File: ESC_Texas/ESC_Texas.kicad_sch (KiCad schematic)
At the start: 77 parts, among them IC1 nRF52840-QFAA-F-R7, IC11 LM3480IM3-3.3_NOPB, IC12 LM3480IM3-3.3_NOPB, J1 RJ45, J11 Battery+, J12 Conn_01x02, J13 Conn_01x04_Pin, J14 Conn_01x01_Pin, J15 Conn_01x01_Pin, J16 Conn_01x01_Pin, J17 Conn_01x01_Pin, J2 BD125-10-A-0305-0580-L-B, J3 Motor, J4 Battery+, P0.10 TestPoint, P0.11 TestPoint, P0.12 TestPoint, P0.7 TestPoint, P0.9 TestPoint, P1.0 TestPoint, P1.1 TestPoint, P1.9 TestPoint, U1 MCP2515-xSO, U2 TJA1051T, X1 CM7V-T1A-32.768kHz, X2 32MHz, X3 C115962

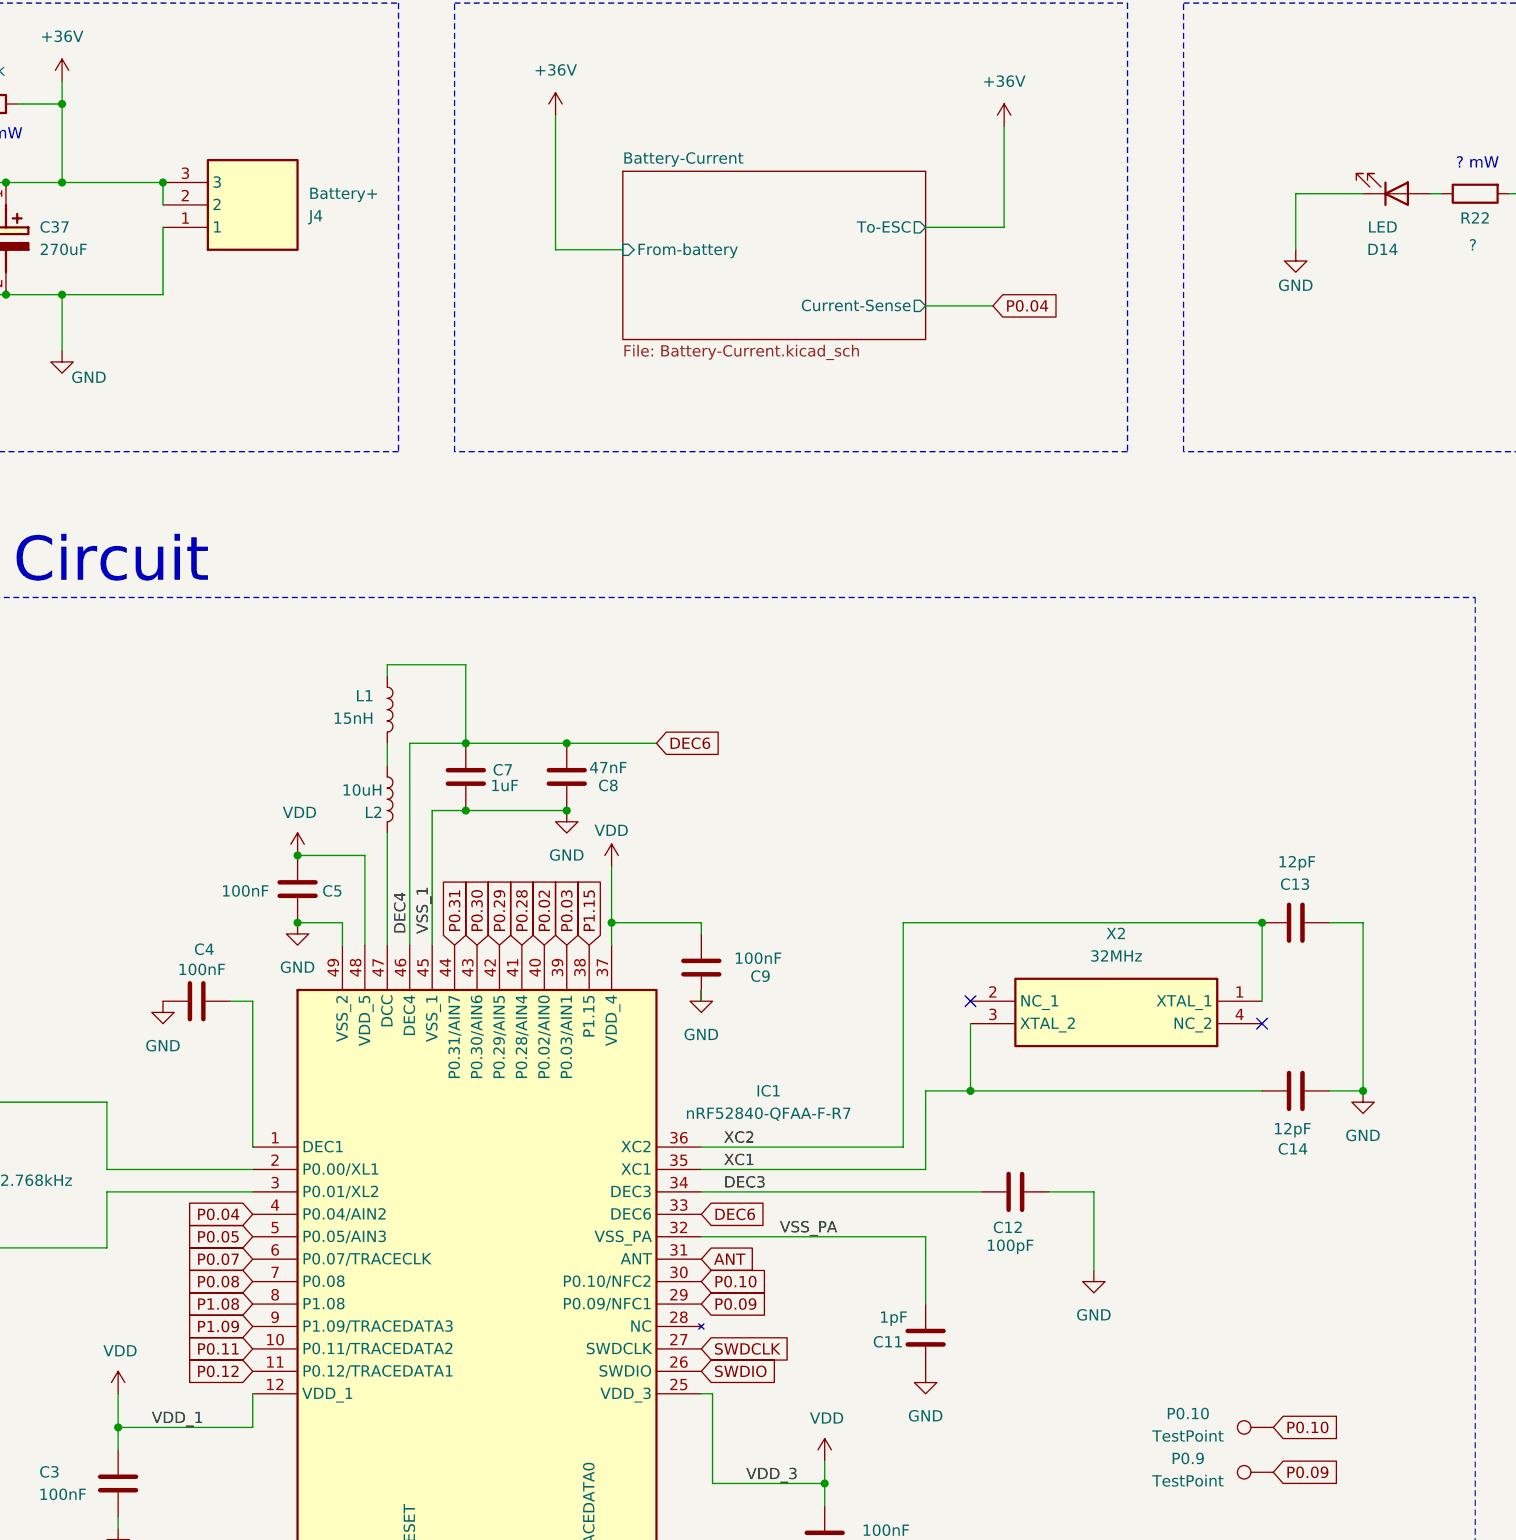
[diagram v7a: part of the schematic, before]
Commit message: Battery connector added
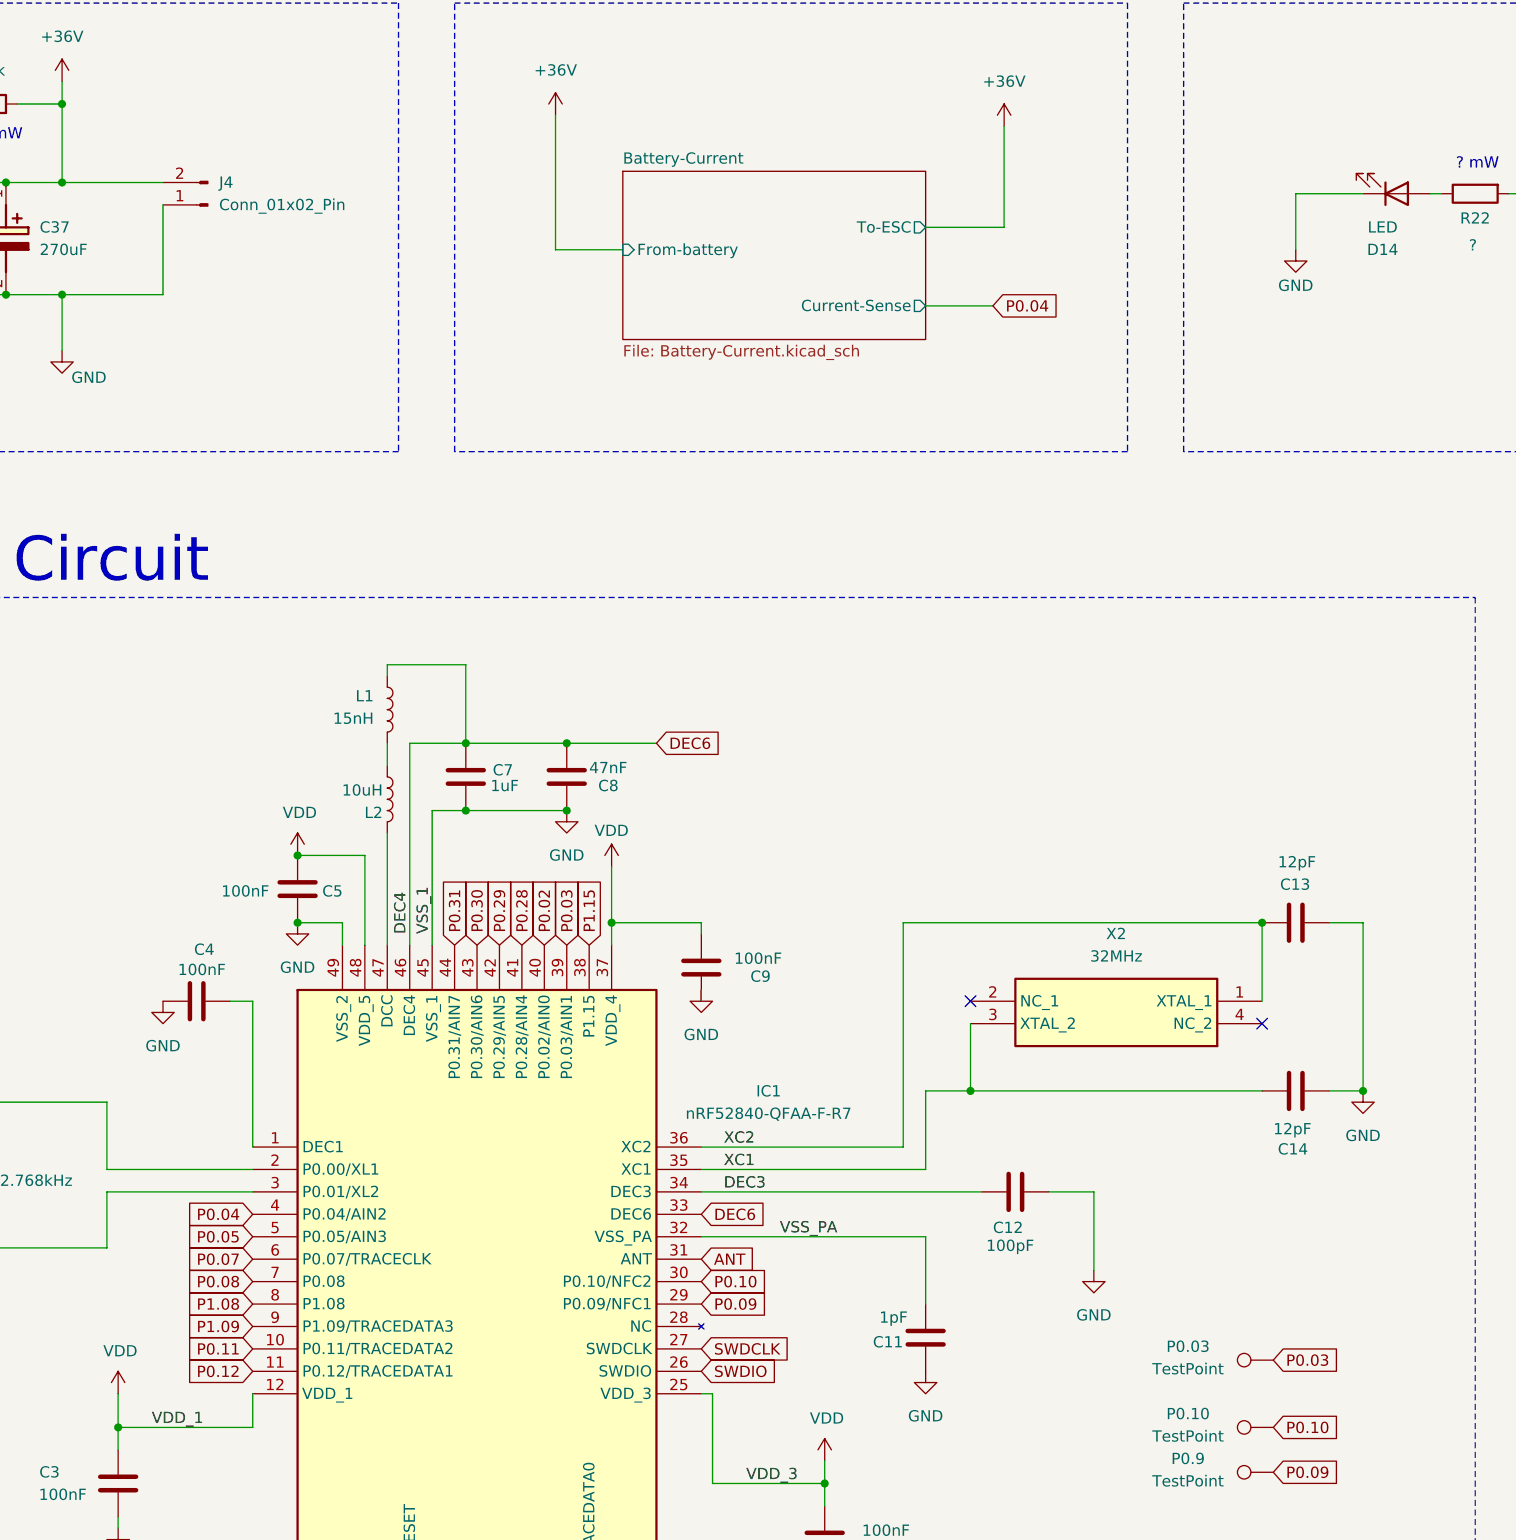
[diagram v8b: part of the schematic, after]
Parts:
- removed J4: Battery+, LIB_2350514-3:SHDRRA3W90P0X350_1X3_1110X920X691P, symbol 2350514-3:2350514-3
- added J4: Conn_01x02_Pin, MP011776:MP011776, symbol Connector:Conn_01x02_Pin
- added P0.03: TestPoint, TestPoint:TestPoint_Pad_D1.0mm, symbol Connector:TestPoint
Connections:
- net +36V: now also J4.2 (Pin_2)
- net GND: now also J4.1 (Pin_1)
- net P0.03: now also P0.03.1
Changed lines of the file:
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@@
 	)
 	(junction
-		(at 106.68 54.61)
-		(diameter 0)
-		(color 0 0 0 0)
-	)
-	(junction
 		(at 140.97 125.73)
 		(diameter 0)
@@
 	(wire
 		(pts
-			(xy 106.68 59.69) (xy 106.68 67.31)
+			(xy 106.68 57.15) (xy 106.68 67.31)
 		)
 		(stroke
@@
 	(wire
 		(pts
-			(xy 106.68 54.61) (xy 106.68 57.15)
-		)
-		(stroke
-			(width 0)
-			(type default)
-		)
-	)
-	(wire
-		(pts
 			(xy 86.36 265.43) (xy 90.17 265.43)
 		)
@@
 		)
 	)
+	(global_label "P0.03"
+		(shape input)
+		(at 232.41 187.96 0)
+		(fields_autoplaced yes)
+		(effects
+			(font
+				(size 1.27 1.27)
+			)
+			(justify left)
+		)
+		(property "Intersheetrefs" "${INTERSHEET_REFS}"
+			(at 240.8985 187.96 0)
+			(effects
+				(font
+					(size 1.27 1.27)
+				)
+				(justify left)
+				(hide yes)
+			)
+		)
+	)
 	(global_label "+5V"
 		(shape input)
@@
 	)
 	(symbol
-		(lib_id "2350514-3:2350514-3")
-		(at 106.68 59.69 0)
-		(mirror x)
-		(unit 1)
-		(exclude_from_sim no)
-		(in_bom yes)
-		(on_board yes)
-		(dnp no)
-		(property "Reference" "J4"
-			(at 123.19 58.4201 0)
-			(effects
-				(font
-					(size 1.27 1.27)
-				)
-				(justify left)
-			)
-		)
-		(property "Value" "Battery+"
-			(at 123.19 55.8801 0)
-			(effects
-				(font
-					(size 1.27 1.27)
-				)
-				(justify left)
-			)
-		)
-		(property "Footprint" "LIB_2350514-3:SHDRRA3W90P0X350_1X3_1110X920X691P"
-			(at 123.19 -35.23 0)
-			(effects
-				(font
-					(size 1.27 1.27)
-				)
-				(justify left top)
-				(hide yes)
-			)
-		)
-		(property "Datasheet" "https://www.te.com/commerce/DocumentDelivery/DDEController?Action=srchrtrv&DocNm=3-1773982-8&DocType=Data%20Sheet&DocLang=English&PartCntxt=2350514-3&DocFormat=pdf"
-			(at 123.19 -135.23 0)
-			(effects
-				(font
-					(size 1.27 1.27)
-				)
-				(justify left top)
-				(hide yes)
-			)
-		)
-		(property "Description" "Body Features: Primary Product Color Green | Product Orientation Right Angle | Configuration Features: Stacking Configuration Side Stackable | Number of Rows 1 | Number of Positions 3 | Contact Features: Contact Mating Area Plating Material Tin | Contact Current Rating (Max) 10 AMP | Contact Base Material Brass | Electrical Characteristics: Operating Voltage 300 VAC | Housing Features: Housing Material PA 66 | Centerline (Pitch) .137 INCH | Centerline (Pitch) 3.5 MM | Mechanical Attachment: Connector Mounti"
-			(at 106.68 59.69 0)
-			(effects
-				(font
-					(size 1.27 1.27)
-				)
-				(hide yes)
-			)
-		)
-		(property "Height" "6.91"
-			(at 123.19 -335.23 0)
-			(effects
-				(font
-					(size 1.27 1.27)
-				)
-				(justify left top)
-				(hide yes)
-			)
-		)
-		(property "Farnell Part Number" ""
-			(at 123.19 -435.23 0)
-			(effects
-				(font
-					(size 1.27 1.27)
-				)
-				(justify left top)
-				(hide yes)
-			)
-		)
-		(property "Farnell Price/Stock" ""
-			(at 123.19 -535.23 0)
-			(effects
-				(font
-					(size 1.27 1.27)
-				)
-				(justify left top)
-				(hide yes)
-			)
-		)
-		(property "Manufacturer_Name" "TE Connectivity"
-			(at 123.19 -635.23 0)
-			(effects
-				(font
-					(size 1.27 1.27)
-				)
-				(justify left top)
-				(hide yes)
-			)
-		)
-		(property "Manufacturer_Part_Number" "2350514-3"
-			(at 123.19 -735.23 0)
-			(effects
-				(font
-					(size 1.27 1.27)
-				)
-				(justify left top)
-				(hide yes)
-			)
-		)
-		(pin "3"
-		)
-		(pin "2"
-		)
-		(pin "1"
-		)
-		(instances
-			(project "ESC_Texas"
-				(path "/0e3a5351-d2cd-4ecc-a1be-cca9c5f62ea0"
-					(reference "J4")
-					(unit 1)
-				)
-			)
-		)
-	)
-	(symbol
 		(lib_id "power:VDD")
 		(at 182.88 246.38 0)
@@
 	)
 	(symbol
+		(lib_id "Connector:Conn_01x02_Pin")
+		(at 111.76 57.15 180)
+		(unit 1)
+		(exclude_from_sim no)
+		(in_bom yes)
+		(on_board yes)
+		(dnp no)
+		(property "Reference" "J4"
+			(at 113.03 54.6099 0)
+			(effects
+				(font
+					(size 1.27 1.27)
+				)
+				(justify right)
+			)
+		)
+		(property "Value" "Conn_01x02_Pin"
+			(at 113.03 57.1499 0)
+			(effects
+				(font
+					(size 1.27 1.27)
+				)
+				(justify right)
+			)
+		)
+		(property "Footprint" "MP011776:MP011776"
+			(at 111.76 57.15 0)
+			(effects
+				(font
+					(size 1.27 1.27)
+				)
+				(hide yes)
+			)
+		)
+		(property "Datasheet" "~"
+			(at 111.76 57.15 0)
+			(effects
+				(font
+					(size 1.27 1.27)
+				)
+				(hide yes)
+			)
+		)
+		(property "Description" "Generic connector, single row, 01x02, script generated"
+			(at 111.76 57.15 0)
+			(effects
+				(font
+					(size 1.27 1.27)
+				)
+				(hide yes)
+			)
+		)
+		(pin "1"
+		)
+		(pin "2"
+		)
+		(instances
+			(project "ESC_Texas"
+				(path "/0e3a5351-d2cd-4ecc-a1be-cca9c5f62ea0"
+					(reference "J4")
+					(unit 1)
+				)
+			)
+		)
+	)
+	(symbol
 		(lib_id "Device:C")
 		(at 140.97 121.92 0)
@@
 					(unit 1)
 				)
+			)
+		)
+	)
+	(symbol
+		(lib_id "Connector:TestPoint")
+		(at 232.41 187.96 90)
+		(unit 1)
+		(exclude_from_sim no)
+		(in_bom yes)
+		(on_board yes)
+		(dnp no)
+		(property "Reference" "P0.03"
+			(at 222.758 186.436 90)
+			(effects
+				(font
+					(size 1.27 1.27)
+				)
+			)
+		)
+		(property "Value" "TestPoint"
+			(at 222.758 188.976 90)
+			(effects
+				(font
+					(size 1.27 1.27)
+				)
+			)
+		)
+		(property "Footprint" "TestPoint:TestPoint_Pad_D1.0mm"
+			(at 232.41 182.88 0)
+			(effects
+				(font
+					(size 1.27 1.27)
+				)
+				(hide yes)
+			)
+		)
+		(property "Datasheet" "~"
+			(at 232.41 182.88 0)
+			(effects
+				(font
+					(size 1.27 1.27)
+				)
+				(hide yes)
+			)
+		)
+		(property "Description" "test point"
+			(at 232.41 187.96 0)
+			(effects
+				(font
+					(size 1.27 1.27)
+				)
+				(hide yes)
+			)
+		)
+		(pin "1"
+		)
+		(instances
+			(project "ESC_Texas"
+				(path "/0e3a5351-d2cd-4ecc-a1be-cca9c5f62ea0"
+					(reference "P0.03")
+					(unit 1)
+				)
